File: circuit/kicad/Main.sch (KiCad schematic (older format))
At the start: 105 parts, among them J1 SH3, J10 PA3, J11 FFC7, J12 SH4, J2 SH3, J3 FFC6, J4 SH6, J5 FTSH2x5, J6 FFC5, J7 SH4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

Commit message: サイドセンサのパターンは完成。メイン基板のフットプリント配置は完了。
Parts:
- removed J6: FFC5, FFC:Molex_0545480571_01x05_P0.5mm, symbol Connector_Generic:Conn_01x05
- J8: renamed from J11; value FFC7 -> FFC12; footprint FFC:Molex_0545480771_01x07_P0.5mm -> Connector_PinHeader_1.00mm:PinHeader_1x12_P1.00mm_Vertical; symbol Connector_Generic:Conn_01x07 -> Connector_Generic:Conn_01x12
- renumbered J12 to J11, J8 to J6
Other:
- note added: "Left\n"
- note added: "Right"
- moved on the sheet: J6

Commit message: パーツ配置まではとりあえず終わらせた。後は配線すればいい。
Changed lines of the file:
@@
 Text Label 9000 12300 0    50   ~ 0
 DRV2_PN
-Text Label 9000 13100 0    50   ~ 0
+Text Label 9000 13400 0    50   ~ 0
 Rotary1
 Text Label 9000 13200 0    50   ~ 0
 Rotary2
+Text Label 9000 13100 0    50   ~ 0
+Rotary4
 Text Label 9000 13300 0    50   ~ 0
-Rotary4
-Text Label 9000 13400 0    50   ~ 0
 Rotary8
 Text Label 9000 13000 0    50   ~ 0

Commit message: hoge
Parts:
- J8: footprint Connector_PinHeader_1.00mm:PinHeader_1x12_P1.00mm_Vertical -> FFC:WürthElektronik_687112183722_01x12_P0.5mm
- U3: footprint ICM-20648:QFN40P300X300X95-24N -> Package_DFN_QFN:QFN-24-1EP_3x3mm_P0.4mm_EP1.75x1.6mm
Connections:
- wire segments 424 -> 428
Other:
- note added: "5V : under 100mA\n3.3V : under 600mA"
- note added: "All : 480mA"
- note added: "All:72mA"
- moved on the sheet: J3
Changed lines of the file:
@@
 F 0 "U3" H 17800 12050 50  0000 C CNN
 F 1 "ICM-20648" H 17800 11950 50  0000 C CNN
-F 2 "ICM-20648:QFN40P300X300X95-24N" H 17800 12000 50  0001 C CNN
+F 2 "Package_DFN_QFN:QFN-24-1EP_3x3mm_P0.4mm_EP1.75x1.6mm" H 17800 12000 50  0001 C CNN
 F 3 "" H 17800 12000 50  0001 C CNN
 	1    17800 12000
@@
 Text Label 4800 9250 0    50   ~ 0
 Sensor04
-Text Label 8200 7850 2    50   ~ 0
-Sensor05
-Text Label 8200 7750 2    50   ~ 0
-Sensor06
-Text Label 8200 7650 2    50   ~ 0
-Sensor07
-Text Label 8200 7550 2    50   ~ 0
+Text Label 8200 7150 2    50   ~ 0
 Sensor08
 Entry Wire Line
@@
 	8200 7250 8300 7150
 Entry Wire Line
-	8200 7350 8300 7250
-Entry Wire Line
-	8200 7450 8300 7350
-Entry Wire Line
-	8200 7550 8300 7450
-Entry Wire Line
-	8200 7650 8300 7550
-Entry Wire Line
 	8200 7750 8300 7650
 Entry Wire Line
 	8200 7850 8300 7750
-Text Label 8200 7450 2    50   ~ 0
+Text Label 4800 9150 0    50   ~ 0
 Sensor09
-Text Label 8200 7350 2    50   ~ 0
+Text Label 4800 9050 0    50   ~ 0
 Sensor10
-Wire Wire Line
-	7650 7450 8200 7450
 Entry Wire Line
 	8200 8850 8300 8750
@@
 L Connector_Generic:Conn_01x06 J3
 U 1 1 620097FD
-P 3950 8950
+P 9250 7450
 AR Path="/620097FD" Ref="J3"  Part="1"
 AR Path="/624FCD7A/620097FD" Ref="J?"  Part="1"
 AR Path="/61F602DC/620097FD" Ref="J?"  Part="1"
 AR Path="/61F60664/620097FD" Ref="J?"  Part="1"
-F 0 "J3" H 3950 8350 50  0000 C CNN
-F 1 "FFC6" H 3950 8450 50  0000 C CNN
-F 2 "FFC:Molex_0545480671_01x06_P0.5mm" H 3950 8950 50  0001 C CNN
-F 3 "~" H 3950 8950 50  0001 C CNN
-	1    3950 8950
-	-1   0    0    -1
+F 0 "J3" H 9250 6850 50  0000 C CNN
+F 1 "FFC6" H 9250 6950 50  0000 C CNN
+F 2 "FFC:Molex_0545480671_01x06_P0.5mm" H 9250 7450 50  0001 C CNN
+F 3 "~" H 9250 7450 50  0001 C CNN
+	1    9250 7450
+	1    0    0    -1
 $EndComp
 $Comp
 L power:+3.3V #PWR063
 U 1 1 62009803
-P 4250 8550
+P 8950 7050
 AR Path="/62009803" Ref="#PWR063"  Part="1"
 AR Path="/624FCD7A/62009803" Ref="#PWR?"  Part="1"
 AR Path="/61F602DC/62009803" Ref="#PWR?"  Part="1"
 AR Path="/61F60664/62009803" Ref="#PWR?"  Part="1"
-F 0 "#PWR063" H 4250 8400 50  0001 C CNN
-F 1 "+3.3V" H 4265 8723 50  0000 C CNN
-F 2 "" H 4250 8550 50  0001 C CNN
-F 3 "" H 4250 8550 50  0001 C CNN
-	1    4250 8550
+F 0 "#PWR063" H 8950 6900 50  0001 C CNN
+F 1 "+3.3V" H 8965 7223 50  0000 C CNN
+F 2 "" H 8950 7050 50  0001 C CNN
+F 3 "" H 8950 7050 50  0001 C CNN
+	1    8950 7050
 	1    0    0    -1
 $EndComp
-Wire Wire Line
-	4250 8750 4150 8750
 $Comp
 L power:GND #PWR066
 U 1 1 6200980A
-P 4250 9450
+P 8950 7950
 AR Path="/6200980A" Ref="#PWR066"  Part="1"
 AR Path="/624FCD7A/6200980A" Ref="#PWR?"  Part="1"
 AR Path="/61F602DC/6200980A" Ref="#PWR?"  Part="1"
 AR Path="/61F60664/6200980A" Ref="#PWR?"  Part="1"
-F 0 "#PWR066" H 4250 9200 50  0001 C CNN
-F 1 "GND" H 4255 9277 50  0000 C CNN
-F 2 "" H 4250 9450 50  0001 C CNN
-F 3 "" H 4250 9450 50  0001 C CNN
-	1    4250 9450
+F 0 "#PWR066" H 8950 7700 50  0001 C CNN
+F 1 "GND" H 8955 7777 50  0000 C CNN
+F 2 "" H 8950 7950 50  0001 C CNN
+F 3 "" H 8950 7950 50  0001 C CNN
+	1    8950 7950
 	1    0    0    -1
 $EndComp
-Wire Wire Line
-	4250 9250 4150 9250
 Text Label 9000 12100 0    50   ~ 0
 DRV1_EN
@@
 	4250 7200 4250 7300
 Wire Wire Line
-	4250 9250 4250 9450
+	8950 7750 8950 7950
 Wire Wire Line
 	6250 8350 4800 8350
@@
 Wire Wire Line
 	9000 13000 9500 13000
-Text Label 5300 10050 0    50   ~ 0
+Text Label 8800 8250 2    50   ~ 0
 LED_R
-Text Label 5300 9950 0    50   ~ 0
+Text Label 8800 8150 2    50   ~ 0
 LED_G
-Text Label 5300 9850 0    50   ~ 0
+Text Label 5300 9750 0    50   ~ 0
 LED_B
 Wire Wire Line
 	7650 8650 9250 8650
-Text Label 8800 8150 2    50   ~ 0
+Text Label 8800 8350 2    50   ~ 0
 Rotary4
-Text Label 8800 8250 2    50   ~ 0
+Text Label 5300 9850 0    50   ~ 0
 Rotary2
-Text Label 8800 8350 2    50   ~ 0
+Text Label 5300 10050 0    50   ~ 0
 Rotary1
-Text Label 8800 10150 2    50   ~ 0
+Text Label 5300 9950 0    50   ~ 0
 Rotary8
 Entry Wire Line
@@
 Wire Wire Line
 	5300 10050 6250 10050
-Text Label 5300 9650 0    50   ~ 0
+Text Label 8800 10150 2    50   ~ 0
 LED_Red
-Text Label 5300 9750 0    50   ~ 0
+Text Label 5300 9650 0    50   ~ 0
 LED_White
 Entry Wire Line
@@
 Text GLabel 7750 9350 2    50   Input ~ 0
 Encorder2_B
-Text Label 8200 7250 2    50   ~ 0
+Text Label 4800 8950 0    50   ~ 0
 Sensor11
-Text Label 8200 7150 2    50   ~ 0
+Text Label 4800 8850 0    50   ~ 0
 Sensor12
 Entry Wire Line
@@
 	7750 10350 7650 10350
 Wire Wire Line
-	4250 8550 4250 8750
-Wire Wire Line
-	4150 8850 6250 8850
-Wire Wire Line
-	4150 8950 6250 8950
-Wire Wire Line
-	4150 9050 6250 9050
-Wire Wire Line
-	4150 9150 6250 9150
+	8950 7050 8950 7250
 Wire Wire Line
 	6150 9450 6250 9450
@@
 	7650 8850 8200 8850
 Wire Wire Line
-	8200 7550 7650 7550
-Wire Wire Line
 	7650 7650 8200 7650
 Wire Wire Line
@@
 $EndComp
 Wire Wire Line
-	8200 7350 7650 7350
-Wire Wire Line
 	7650 8150 8800 8150
 Wire Wire Line
@@
 F 0 "J8" H 9700 13700 50  0000 C CNN
 F 1 "FFC12" V 9800 13300 50  0000 C CNN
-F 2 "Connector_PinHeader_1.00mm:PinHeader_1x12_P1.00mm_Vertical" H 9700 13100 50  0001 C CNN
+F 2 "FFC:WürthElektronik_687112183722_01x12_P0.5mm" H 9700 13100 50  0001 C CNN
 F 3 "~" H 9700 13100 50  0001 C CNN
 	1    9700 13100
@@
 Text Notes 12700 7100 0    50   ~ 0
 Left\n
-Wire Bus Line
-	4700 9350 4700 11000
+Text Label 8200 7850 2    50   ~ 0
+Sensor05
+Text Label 8200 7750 2    50   ~ 0
+Sensor06
+Text Label 8200 7250 2    50   ~ 0
+Sensor07
+Wire Wire Line
+	4800 8850 6250 8850
+Wire Wire Line
+	4800 8950 6250 8950
+Wire Wire Line
+	4800 9050 6250 9050
+Wire Wire Line
+	4800 9150 6250 9150
+Entry Wire Line
+	4700 8950 4800 8850
+Entry Wire Line
+	4700 9050 4800 8950
+Entry Wire Line
+	4700 9150 4800 9050
+Entry Wire Line
+	4700 9250 4800 9150
+Wire Wire Line
+	8950 7250 9050 7250
+Wire Wire Line
+	9050 7750 8950 7750
+Wire Wire Line
+	8200 7650 8200 7600
+Wire Wire Line
+	8200 7600 8400 7600
+Wire Wire Line
+	8400 7600 8400 7650
+Wire Wire Line
+	8400 7650 9050 7650
+Wire Wire Line
+	7650 7550 9050 7550
+Wire Wire Line
+	7650 7450 9050 7450
+Wire Wire Line
+	7650 7350 9050 7350
 Wire Bus Line
 	19750 5950 19750 8850
@@
 	8300 5850 19650 5850
 Wire Bus Line
+	8300 5850 8300 11000
+Wire Bus Line
 	8900 8250 8900 11200
 Wire Bus Line
-	5200 8550 5200 11200
+	4700 8950 4700 11000
 Wire Bus Line
-	8300 5850 8300 11000
+	5200 8550 5200 11200
 Wire Bus Line
 	8900 11200 8900 13600
+Text Notes 15050 2000 0    50   ~ 0
+20mA
+Text Notes 18100 1500 0    50   ~ 0
+All : 480mA
+Text Notes 12650 6250 0    50   ~ 0
+All:72mA
+Text Notes 6150 12400 0    50   ~ 0
+5V : under 100mA\n3.3V : under 600mA
 $EndSCHEMATC

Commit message: hoge
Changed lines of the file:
@@
 Text Label 9000 13300 0    50   ~ 0
 Rotary8
-Text Label 9000 13000 0    50   ~ 0
+Text Label 9000 12800 0    50   ~ 0
 LED_R
 Text Label 9000 12900 0    50   ~ 0
 LED_G
-Text Label 9000 12800 0    50   ~ 0
+Text Label 9000 13000 0    50   ~ 0
 LED_B
 Entry Wire Line
@@
 Wire Wire Line
 	7650 7350 9050 7350
+Text Notes 15050 2000 0    50   ~ 0
+20mA
+Text Notes 18100 1500 0    50   ~ 0
+All : 480mA
+Text Notes 12650 6250 0    50   ~ 0
+All:72mA
+Text Notes 6150 12400 0    50   ~ 0
+5V : under 100mA\n3.3V : under 600mA
 Wire Bus Line
 	19750 5950 19750 8850
@@
 Wire Bus Line
 	8900 11200 8900 13600
-Text Notes 15050 2000 0    50   ~ 0
-20mA
-Text Notes 18100 1500 0    50   ~ 0
-All : 480mA
-Text Notes 12650 6250 0    50   ~ 0
-All:72mA
-Text Notes 6150 12400 0    50   ~ 0
-5V : under 100mA\n3.3V : under 600mA
 $EndSCHEMATC

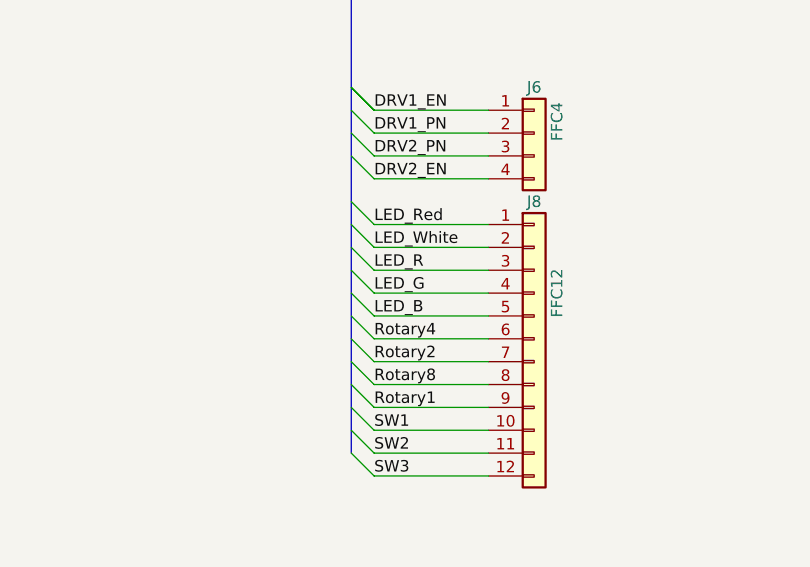
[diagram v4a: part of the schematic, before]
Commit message: あとはシルクを見やすい位置にもっていくだけ。
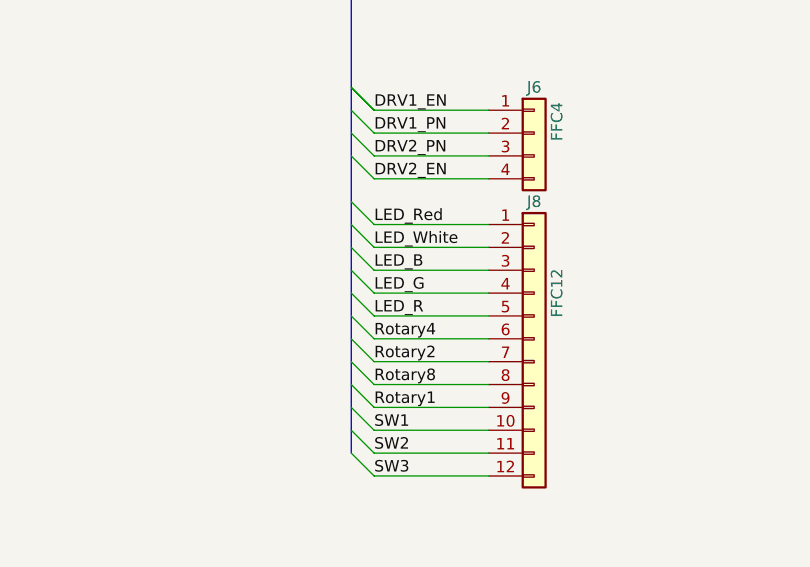
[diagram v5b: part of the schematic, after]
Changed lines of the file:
@@
 Text Label 9000 13300 0    50   ~ 0
 Rotary8
-Text Label 9000 12800 0    50   ~ 0
+Text Label 9000 13000 0    50   ~ 0
 LED_R
 Text Label 9000 12900 0    50   ~ 0
 LED_G
-Text Label 9000 13000 0    50   ~ 0
+Text Label 9000 12800 0    50   ~ 0
 LED_B
 Entry Wire Line
